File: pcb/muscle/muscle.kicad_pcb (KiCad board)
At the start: 4 copper layers, 125 x 54 mm, 153 parts, among them J1 B4B-XH-2(LF)(SN), J10 USB4115-03-C, J2 ZX-SH1.0-3PLT, J4 ZX-SH1.0-3PLT, J5 B4B-XH-2(LF)(SN), J8 B2B-XH-A(LF)(SN), J9 USB4115-03-C, Q3 WSD6070DN56, Q4 WSD6070DN56, Q5 BSS138W, Q6 WSD6070DN56, Q7 AGM18N10AP, Q8 WSD6070DN56, SW1 TS3425BA, SW2 TS3425BA, U1 TMC2209-LA, U10 TPS62933, U13 TLV75733PDBV, U14 DRV8701P, U2 TMC2209-LA, U3 RP2350A, U4 TPS92692PWP, U6 W25Q128JVSS, U7 TPS25730AD, Y1 ABM8-272-T3

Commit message: wip: tweaks
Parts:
- moved TP3 29.5 mm to (160.0, 98.3)
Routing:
- net /X_DIAG: track 113.2 -> 111.4 mm
- net +3V3: track 139.1 -> 137.4 mm
- net Net-(U2-5VOUT): track 12.9 -> 11.4 mm
- net /STEP_UART: track 135.5 -> 134.0 mm
- net /X_STEP: track 111.2 -> 109.7 mm
- net /X_DIR: track 113.5 -> 112.1 mm
- net /S_IMON: track 92.5 -> 91.8 mm
- net GND: vias 285 -> 273

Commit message: wip: muscle: tweaks
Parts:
- removed C69: 10u, Capacitor_SMD:C_0402_1005Metric
- moved TP3 28.1 mm to (139.7, 78.8)
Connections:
- U7 pad 38: Net-(U7-VIN_3V3) -> GND
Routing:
- net /USB_D-: track 24.0 -> 26.4 mm
- net Net-(U7-VIN_3V3): track 2.38 -> 0.00 mm
- net GND: track 136.6 -> 138.3 mm, vias 273 -> 272
- net /USB_D+: track 21.9 -> 20.4 mm, vias 2 -> 1

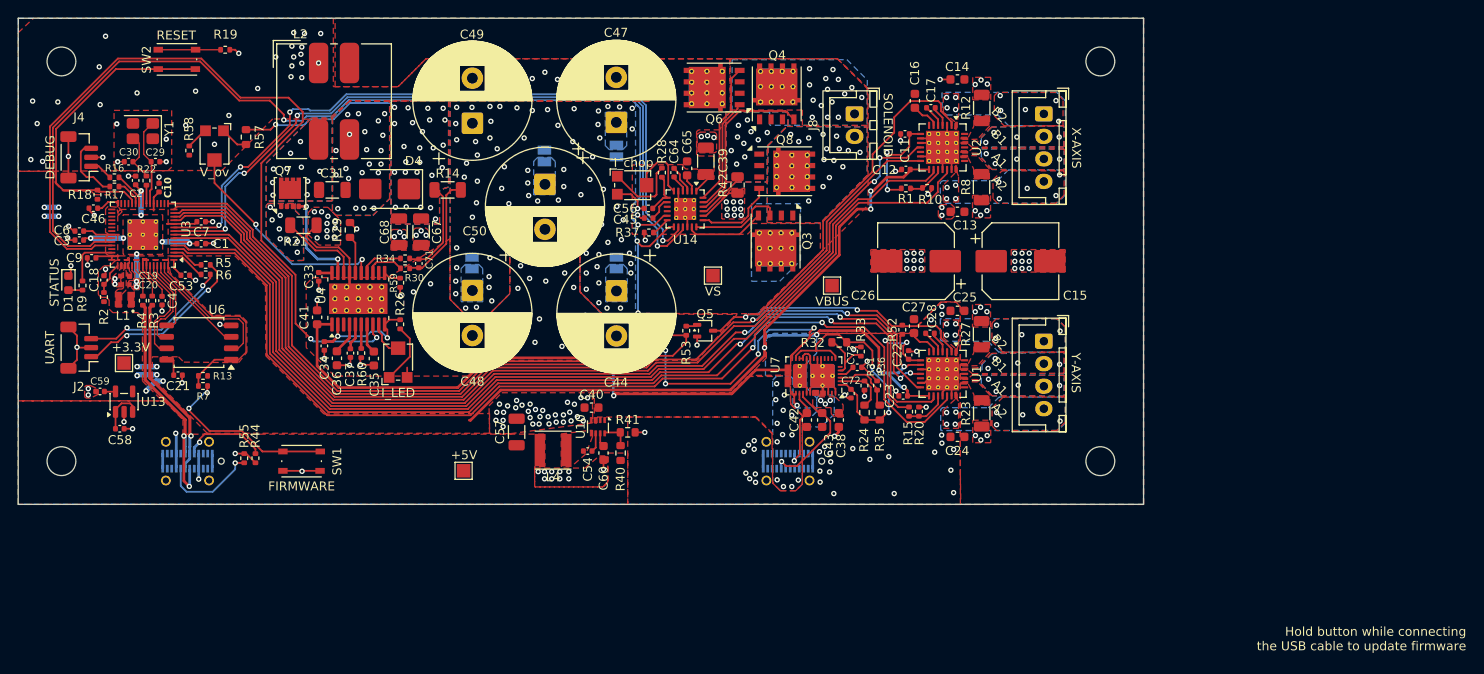
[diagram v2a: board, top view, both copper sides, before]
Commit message: pcb: limit solenoid input current, not output current
Input current is what we care about to keep the USB PD supply happy,
whereas the output current should be as high as the input current allows
to charge the solenoid capacitors as quickly as possible.
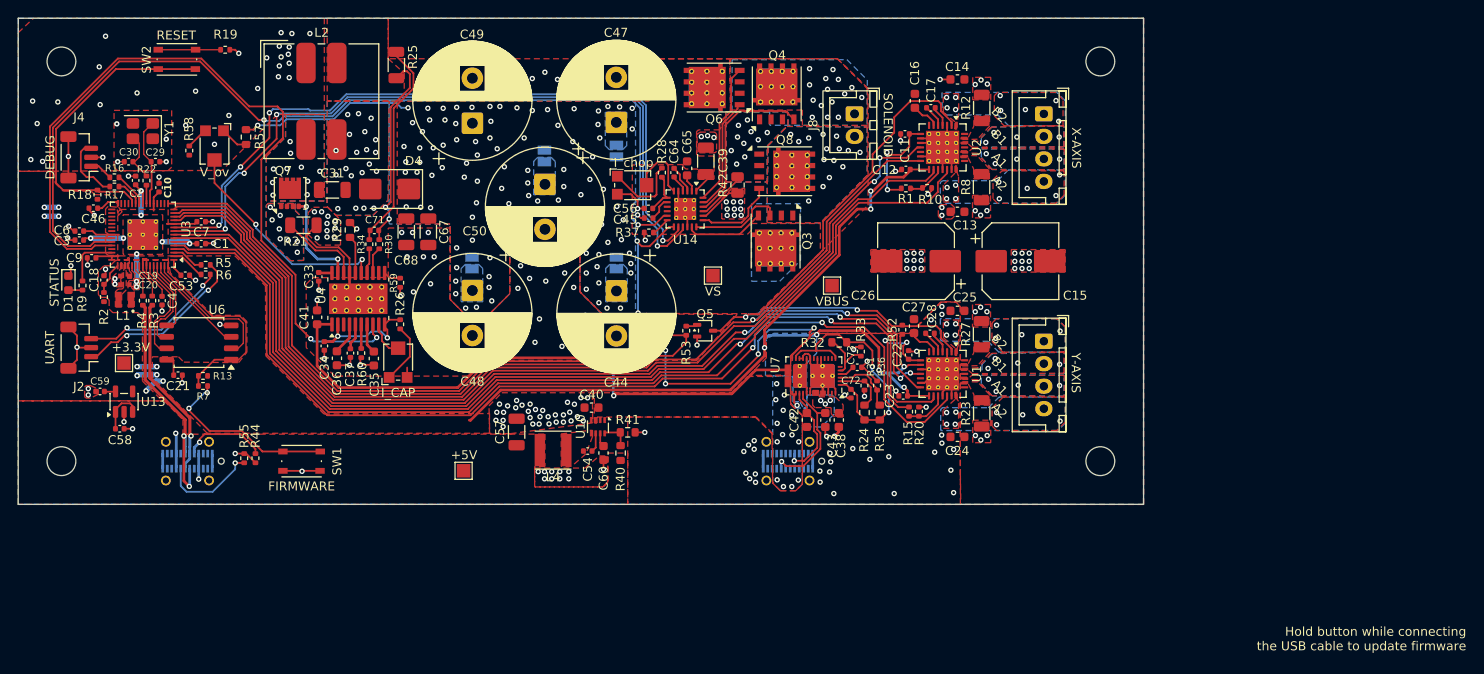
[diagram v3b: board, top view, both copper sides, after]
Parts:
- removed R14: 120m,1%,1W, Resistor_SMD:R_1206_3216Metric
- added R25: 50m,1%,1W, Resistor_SMD:R_1206_3216Metric, F.Cu at (91.3, 54.3)
- RV1: value I_LED -> I_CAP
- moved C71 6.15 mm to (88.9, 72.7), turned to 0 degrees
- moved R34 4.27 mm to (88.3, 74.2), turned to 90 degrees
- moved R30 3.93 mm to (89.4, 74.2), turned to 90 degrees
- moved L2 1.40 mm to (83.0, 58.3)
- moved C68 0.80 mm to (92.4, 72.8)
- moved C67 0.80 mm to (94.8, 72.8)
- moved C43 0.35 mm to (138.9, 93.7)
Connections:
- net Net-(U4-CSN) renamed /S_CS-
- net Net-(U4-CSP) renamed /S_CS+
- C67 pad 1: Net-(D4-K) -> VS
- C68 pad 1: Net-(D4-K) -> VS
- C71 pad 1: Net-(D4-K) -> VBUS
- C71 pad 2: VS -> Net-(C71-Pad2)
- D4 pad 1: Net-(D4-K) -> VS
- L2 pad 2: VBUS -> Net-(C71-Pad2)
- R30 pad 2: VS -> Net-(C71-Pad2)
- R34 pad 2: Net-(D4-K) -> VBUS
- R57 pad 1: Net-(D4-K) -> VS
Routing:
- net Net-(D4-K): track 28.4 -> 0.00 mm, vias 26 -> 0
- net VBUS: track 66.7 -> 90.3 mm
- net Net-(C71-Pad2): track 0.00 -> 22.1 mm, vias 0 -> 2
- net VS: track 15.0 -> 22.0 mm, vias 76 -> 97
- net /S_IMON: track 91.8 -> 88.7 mm
- net /S_CS+: track 4.84 -> 2.79 mm
- net /CC1: track 9.23 -> 10.9 mm
- net /S_CS-: track 4.30 -> 2.97 mm
- net /S_IN1: track 82.0 -> 83.2 mm
- net GND: track 138.3 -> 139.5 mm, vias 272 -> 270
- net /S_IN2: track 80.8 -> 81.6 mm
- net VBUS0: vias 16 -> 17
- net Net-(D4-A): vias 21 -> 20
- added copper zone on F.Cu, net Net-(C71-Pad2)
- added copper zone on In1.Cu, net VBUS0
- added copper zone on In2.Cu, net VBUS0
- removed copper zone on B.Cu, net Net-(D4-K)
- removed copper zone on F.Cu, net Net-(D4-K)
- removed copper zone on In1.Cu, net Net-(D4-K)
- removed copper zone on In2.Cu, net Net-(D4-K)

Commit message: pcb/muscle: tweaks
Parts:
- moved R19 2.50 mm to (72.3, 55.1)
- moved SW2 2.50 mm to (66.9, 56.2)
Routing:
- net /S_IMON: track 88.7 -> 86.6 mm
- net /S_SENSE: track 108.5 -> 106.4 mm
- net /RESET: track 33.9 -> 32.8 mm

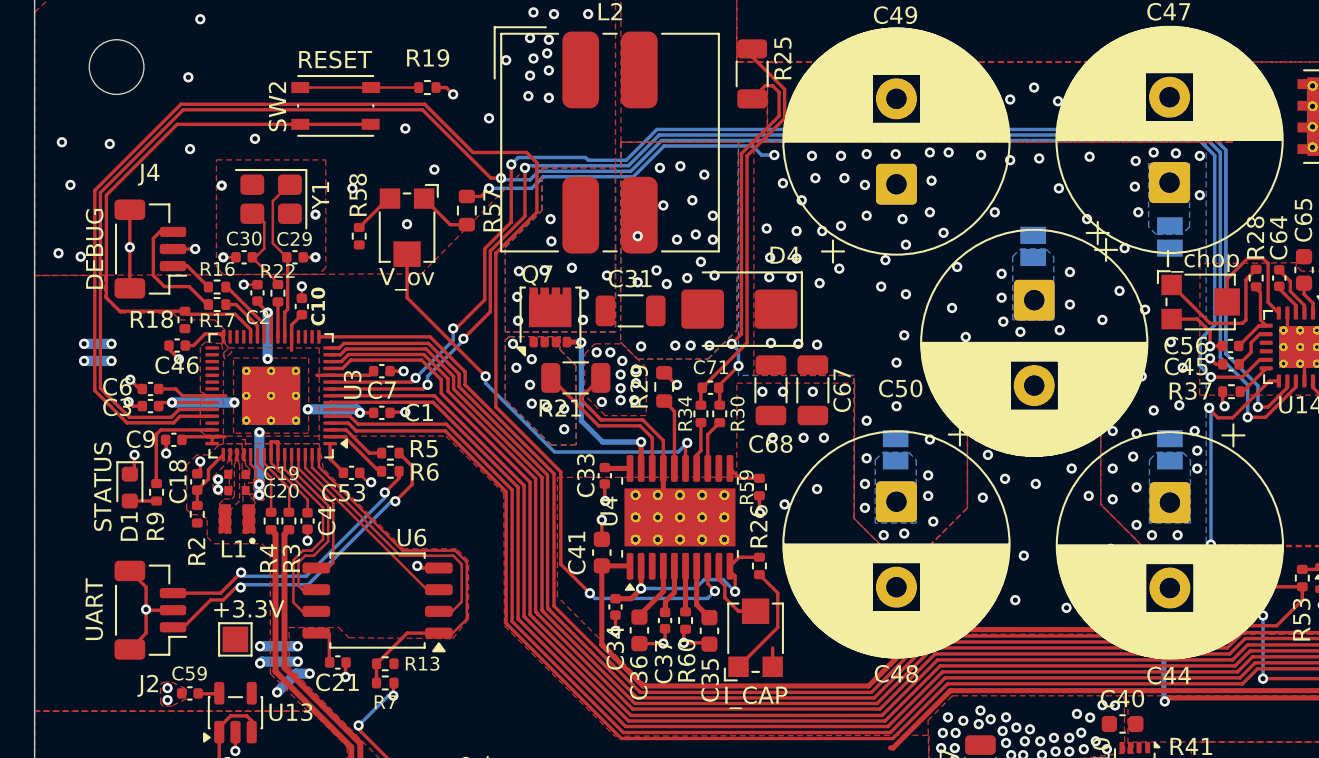
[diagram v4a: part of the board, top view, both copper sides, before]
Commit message: pcb/muscle: add testpoints for measuring currents
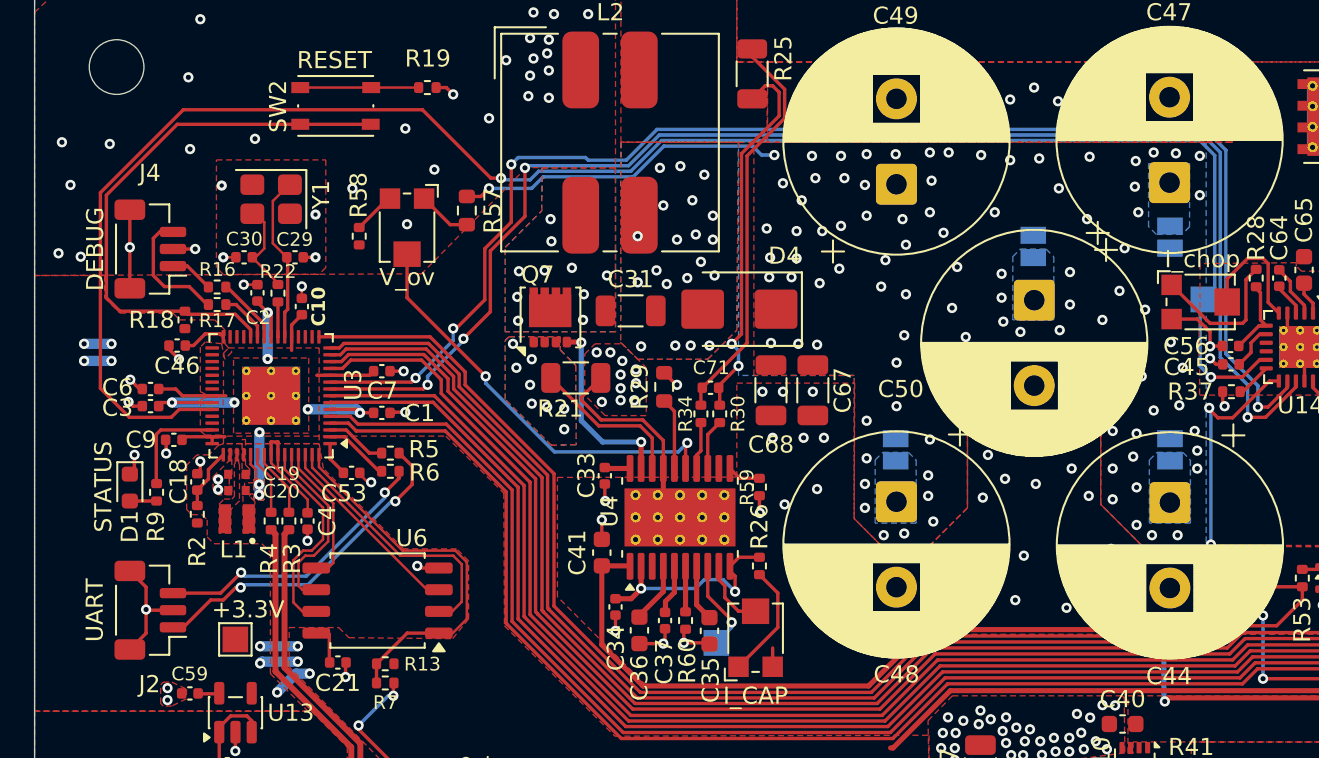
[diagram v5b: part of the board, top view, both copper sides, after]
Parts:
- added TP5: S_IMON, TestPoint:TestPoint_Pad_1.5x1.5mm, B.Cu at (89.2, 87.6)
- added TP6: S_SENSE, TestPoint:TestPoint_Pad_1.5x1.5mm, B.Cu at (117.7, 67.5)
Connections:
- U3 pad 41: /S_IMON -> unconnected-(U3-GPIO27/ADC1-Pad41)
- U4 pad 8: /S_IMON -> Net-(U4-IMON)
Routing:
- net /S_IMON: track 86.6 -> 0.00 mm, vias 2 -> 0
- net Net-(U4-IMON): track 0.00 -> 5.43 mm, vias 0 -> 1
